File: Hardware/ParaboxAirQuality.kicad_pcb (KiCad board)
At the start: 2 copper layers, 19 parts, among them J1 USB_B_Mini, J2 Conn_01x03, J3 Conn_01x04, M1 CC2538MODULE, U1 ST1S10PHR, U2 M25PX32-VMW

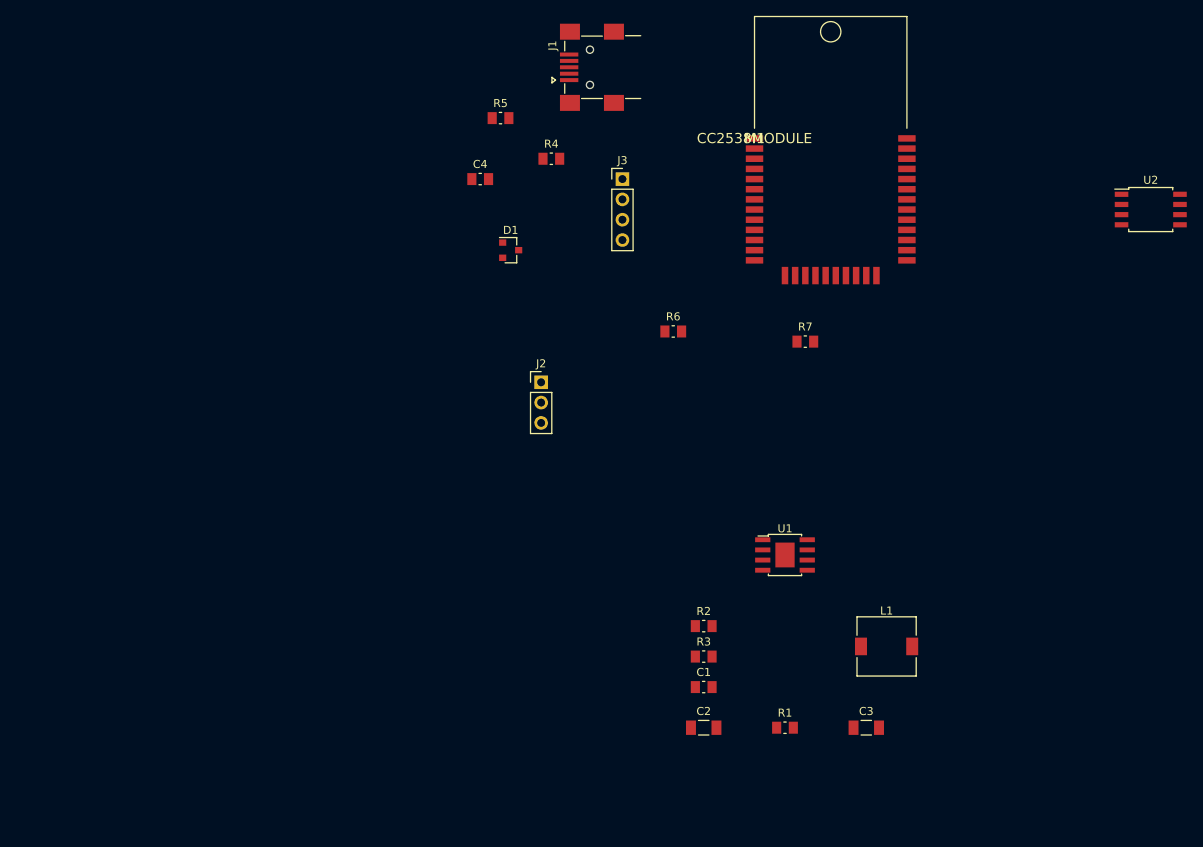
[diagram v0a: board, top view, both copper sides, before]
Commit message: rename libs
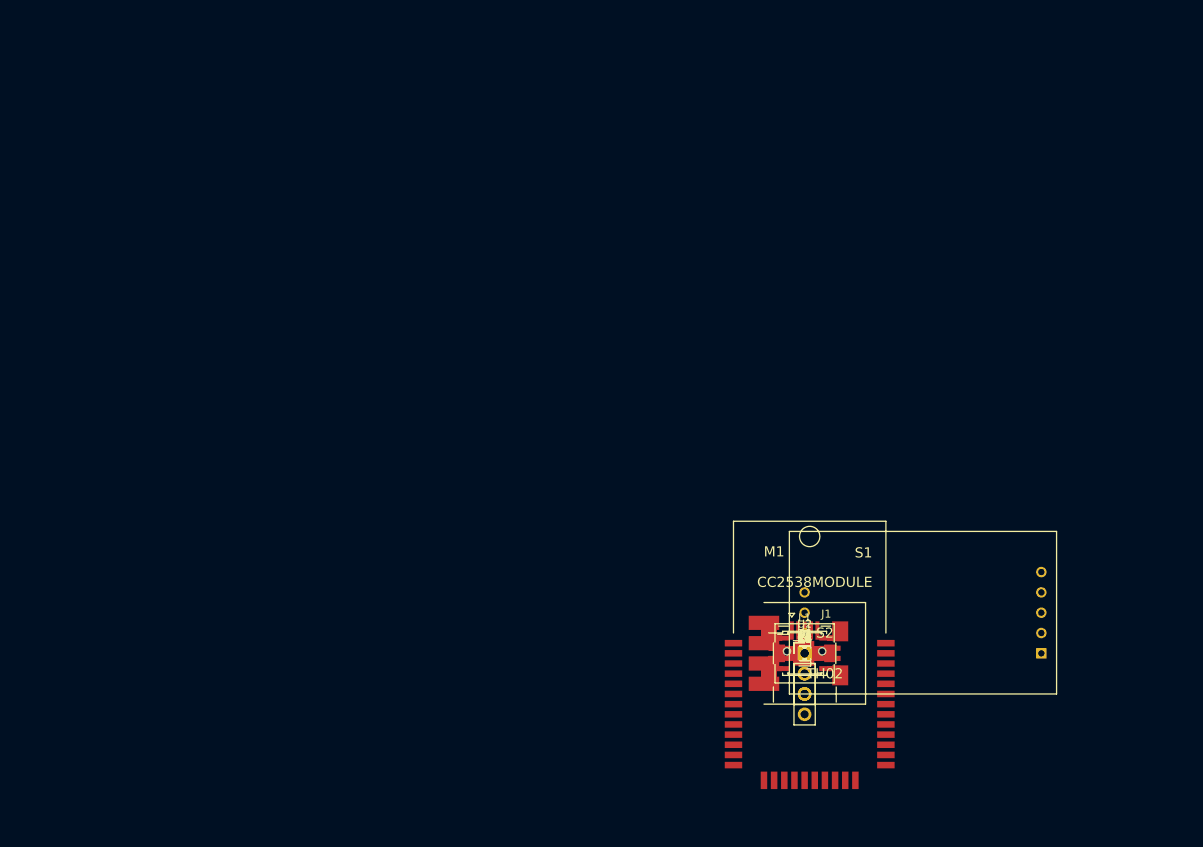
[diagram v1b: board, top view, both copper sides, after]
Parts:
- added C5, C6: 47p, Capacitor_SMD:C_0805_2012Metric_Pad1.15x1.50mm_HandSolder, F.Cu at (148.5, 105.0)
- added R8, R9: 10k, Resistor_SMD:R_0805_2012Metric_Pad1.15x1.50mm_HandSolder, F.Cu at (148.5, 105.0)
- added S1: MH-Z19, Levap_Sensors:MH-Z19, F.Cu at (148.5, 105.0)
- added S2: TH02, Levap_Sensors:TH02MOD, F.Cu at (148.5, 105.0)
- M1: footprint 0_levap_rf:0_levap_rf-CC2538MODULE -> Levap_RF_Modules:CC2538MOD
- moved J1 77.9 mm to (148.5, 105.0), turned to 0 degrees
- moved R5 76.9 mm to (148.5, 105.0)
- moved C4 71.8 mm to (148.5, 105.0)
- moved U2 70.4 mm to (148.5, 105.0)
- moved R4 69.5 mm to (148.5, 105.0)
- moved M1 64.7 mm to (148.5, 105.0)
- moved J3 63.5 mm to (148.5, 105.0)
- moved D1 62.4 mm to (148.5, 105.0)
- moved J2 47.2 mm to (148.5, 105.0)
- moved R6 43.5 mm to (148.5, 105.0)
- moved R7 39.0 mm to (148.5, 105.0)
- moved C2 15.7 mm to (148.5, 105.0)
- moved C1 13.3 mm to (148.5, 105.0)
- moved R2 13.1 mm to (148.5, 105.0)
- moved R3 12.6 mm to (148.5, 105.0)
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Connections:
- J3 pad 2: /UART0_RX -> /UART0_BOOT_RX
- J3 pad 3: /UART0_TX -> /UART0_BOOT_TX
- M1 pad 16: Net-(M1-Pad16) -> /CO2_PWM
- M1 pad 17: Net-(M1-Pad17) -> /UART0_RX
- M1 pad 18: Net-(M1-Pad18) -> /UART0_TX
- M1 pad 19: Net-(M1-Pad19) -> /I2C_SDA
- M1 pad 20: Net-(M1-Pad20) -> /I2C_SCK
- M1 pad 22: /UART0_RX -> /UART0_BOOT_RX
- M1 pad 23: /UART0_TX -> /UART0_BOOT_TX

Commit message: Final release 1.0, add gerbers
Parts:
- removed D1: BAT54C, Package_TO_SOT_SMD:SOT-23
- added C10: 0.1u, Capacitor_SMD:C_0805_2012Metric_Pad1.15x1.50mm_HandSolder, B.Cu at (117.2, 59.8)
- added C7: 0.1u, Capacitor_SMD:C_0805_2012Metric_Pad1.15x1.50mm_HandSolder, F.Cu at (73.8, 86.2)
- added C8: 0.1u, Capacitor_SMD:C_0805_2012Metric_Pad1.15x1.50mm_HandSolder, F.Cu at (83.2, 101.8)
- added C9: CP, Capacitor_SMD:CP_Elec_10x10, F.Cu at (84.2, 93.5)
- added J4: Conn_01x03, Connector_PinHeader_2.54mm:PinHeader_1x03_P2.54mm_Vertical, F.Cu at (85.8, 81.0)
- added J5: BOOT, Connector_PinHeader_2.54mm:PinHeader_1x02_P2.54mm_Vertical, F.Cu at (97.5, 106.8)
- added J6: I2C, Connector_PinHeader_2.54mm:PinHeader_1x04_P2.54mm_Vertical, F.Cu at (100.0, 112.5)
- added J7: BEEP, Connector_PinHeader_2.54mm:PinHeader_1x02_P2.54mm_Vertical, F.Cu at (119.2, 106.8)
- added J8: MISC, Connector_PinHeader_2.54mm:PinHeader_2x07_P2.54mm_Vertical, F.Cu at (101.0, 75.5)
- added R10: 10k, Resistor_SMD:R_0805_2012Metric_Pad1.15x1.50mm_HandSolder, F.Cu at (64.8, 112.2)
- added R11: 120, Resistor_SMD:R_0805_2012Metric_Pad1.15x1.50mm_HandSolder, B.Cu at (103.8, 64.5)
- added R12: 10k, Resistor_SMD:R_0805_2012Metric_Pad1.15x1.50mm_HandSolder, F.Cu at (122.0, 111.5)
- added REF**: MountingHole_2.7mm_M2.5, MountingHole:MountingHole_2.7mm_M2.5, F.Cu at (52.5, 67.0)
- added REF**: MountingHole_2.7mm_M2.5, MountingHole:MountingHole_2.7mm_M2.5, F.Cu at (122.5, 67.0)
- added REF**: MountingHole_2.7mm_M2.5, MountingHole:MountingHole_2.7mm_M2.5, F.Cu at (87.5, 118.0)
- added S3: CJMCU-811, Levap_Sensors:CJMCU-811, F.Cu at (60.0, 111.0)
- added S4: BMP280MOD, Levap_Sensors:BMP280MOD, F.Cu at (80.0, 113.5)
- added SW1: SW_Push, Button_Switch_THT:SW_Tactile_SPST_Angled_PTS645Vx83-2LFS, F.Cu at (122.0, 117.0)
- added U3: LM1117-3.3, Package_TO_SOT_SMD:TO-252-2, F.Cu at (73.5, 93.8)
- added U4: MAX3072E, Package_SO:SOIC-8_3.9x4.9mm_P1.27mm, B.Cu at (112.2, 58.0)
- C4, R7, U2: moved to B.Cu
- J2: value Conn_01x03 -> VIN; footprint Connector_PinHeader_2.54mm:PinHeader_1x03_P2.54mm_Vertical -> Connector_Phoenix_MC:PhoenixContact_MC_1,5_4-G-5.08_1x04_P5.08mm_Horizontal
- J3: value Conn_01x04 -> BOOT
- L1: footprint Inductors_SMD:L_7.3x7.3_H4.5 -> Inductor_SMD:L_7.3x7.3_H4.5
- R2: value 62.5k -> 105k
- moved J1 92.7 mm to (56.5, 93.5), turned to 270 degrees
- moved R4 86.1 mm to (62.8, 97.2), turned to 90 degrees
- moved R6 85.9 mm to (63.8, 90.8)
- moved R2 85.9 mm to (80.0, 53.2), turned to 270 degrees
- moved C6 85.7 mm to (64.8, 87.0), turned to 90 degrees
- moved R5 85.6 mm to (63.8, 93.2)
- moved C5 83.4 mm to (65.5, 97.2), turned to 270 degrees
- moved R3 83.4 mm to (80.0, 57.5), turned to 270 degrees
- moved S1 80.4 mm to (71.5, 82.0), turned to 90 degrees
- moved R1 80.1 mm to (86.5, 54.2), turned to 180 degrees
- moved C1 78.3 mm to (80.5, 66.2), turned to 90 degrees
- moved U1 76.9 mm to (85.2, 61.2), turned to 270 degrees
- moved C2 73.0 mm to (86.0, 67.2)
- moved C3 70.3 mm to (91.2, 64.2), turned to 180 degrees
- moved L1 67.3 mm to (89.2, 73.0)
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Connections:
- C1 pad 1: Vin -> VCC
- C2 pad 1: Vin -> VCC
- C3 pad 1: +3V3 -> /Vin_5V
- J2 pad 1: /EXT_Vin -> VCC
- J2 pad 2: Vin -> GND
- J2 pad 3: /USB_5V -> /RS485_A
- J3 pad 1: GND -> +3V3
- J3 pad 2: /UART0_BOOT_RX -> GND
- J3 pad 4: +3V3 -> /UART0_BOOT_RX
- L1 pad 2: +3V3 -> /Vin_5V
- M1 pad 10: Net-(M1-Pad10) -> /UART1_TX
- M1 pad 11: Net-(M1-Pad11) -> /RS485_RE-DE
- M1 pad 15: Net-(M1-Pad15) -> /CCS811_WAK
- M1 pad 19: /I2C_SDA -> /JOIN_BUT
- M1 pad 20: /I2C_SCK -> /BEEP
- M1 pad 29: Net-(M1-Pad29) -> /I2C_SCK
- M1 pad 3: Net-(M1-Pad3) -> /TMS
- M1 pad 30: Net-(M1-Pad30) -> /I2C_SDA
- M1 pad 32: Net-(M1-Pad32) -> /PD1
- M1 pad 33: Net-(M1-Pad33) -> /RESET
- M1 pad 34: Net-(M1-Pad34) -> /PD3
- M1 pad 35: Net-(M1-Pad35) -> /PD4
- M1 pad 4: Net-(M1-Pad4) -> /TCK
- M1 pad 5: Net-(M1-Pad5) -> /TDO/PB7
- M1 pad 6: Net-(M1-Pad6) -> /TDI/PB6
- M1 pad 7: Net-(M1-Pad7) -> /PB5
- M1 pad 8: Net-(M1-Pad8) -> /PB4
- M1 pad 9: Net-(M1-Pad9) -> /UART1_RX
- R1 pad 1: Vin -> VCC
- R2 pad 1: +3V3 -> /Vin_5V
- S1 pad 6: +3V3 -> +5V
- U1 pad 1: Vin -> VCC
- U1 pad 6: Vin -> VCC
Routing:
- net +3V3: track 0.00 -> 214.9 mm, vias 0 -> 3
- net VCC: track 0.00 -> 103.9 mm, vias 0 -> 5
- net /I2C_SDA: track 0.00 -> 94.4 mm, vias 0 -> 1
- net /I2C_SCK: track 0.00 -> 88.5 mm, vias 0 -> 1
- net +5V: track 0.00 -> 59.6 mm
- net /CCS811_WAK: track 0.00 -> 59.4 mm, vias 0 -> 2
- net /UART0_RX: track 0.00 -> 51.2 mm, vias 0 -> 1
- net /JOIN_BUT: track 0.00 -> 50.2 mm, vias 0 -> 2
- net /UART0_TX: track 0.00 -> 49.9 mm, vias 0 -> 1
- net /USB_P: track 0.00 -> 45.2 mm, vias 0 -> 2
- net /RS485_RE-DE: track 0.00 -> 43.8 mm, vias 0 -> 1
- net /USB_N: track 0.00 -> 40.1 mm, vias 0 -> 2
- net /USB_PULL: track 0.00 -> 39.9 mm, vias 0 -> 2
- net /UART1_RX: track 0.00 -> 39.4 mm, vias 0 -> 1
- net /BEEP: track 0.00 -> 38.7 mm, vias 0 -> 1
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- added copper zone on F.Cu, net +3V3
- added copper zone on F.Cu, net /Vin_5V
- added copper zone on B.Cu, net GND
- added copper zone on F.Cu, net GND
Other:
- board outline added: 75 x 74 mm
- board text added: "Air Quality 1.0"
- board text added: "parabox.org"
